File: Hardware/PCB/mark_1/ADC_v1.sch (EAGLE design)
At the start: 17 parts, among them IC1 MCP3424, IC2 MCP23017SO, Q1 IRLML6402, Q2 IRLML6402, Q3 IRLML6402, Q4 IRLML6402

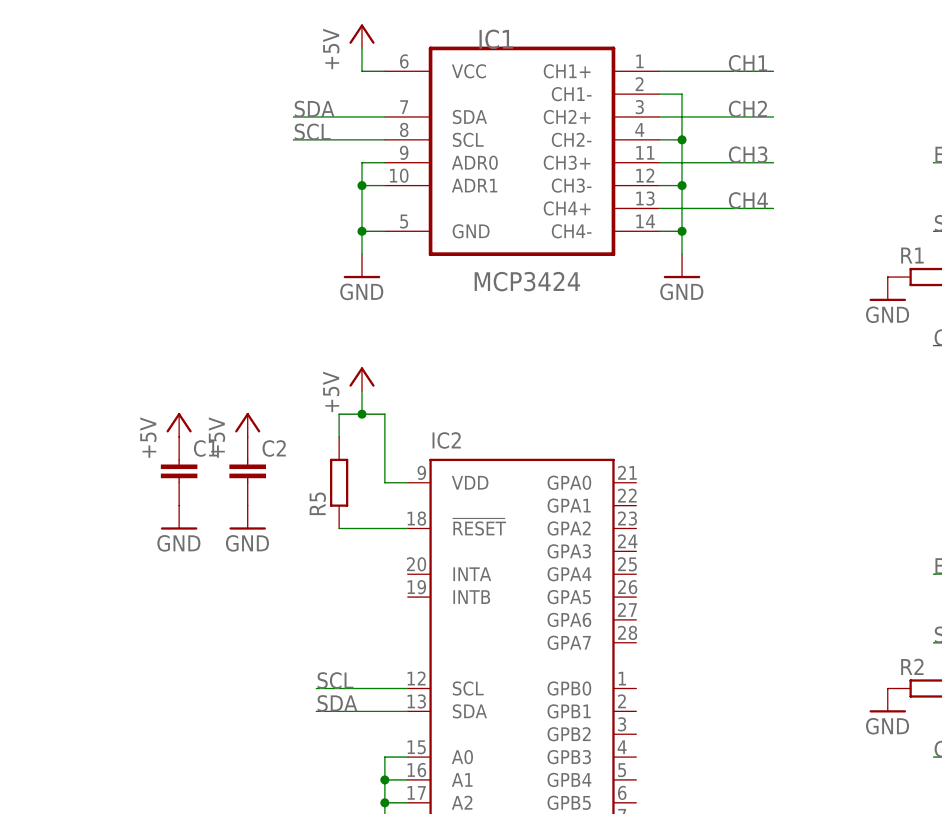
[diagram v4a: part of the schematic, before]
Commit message: 
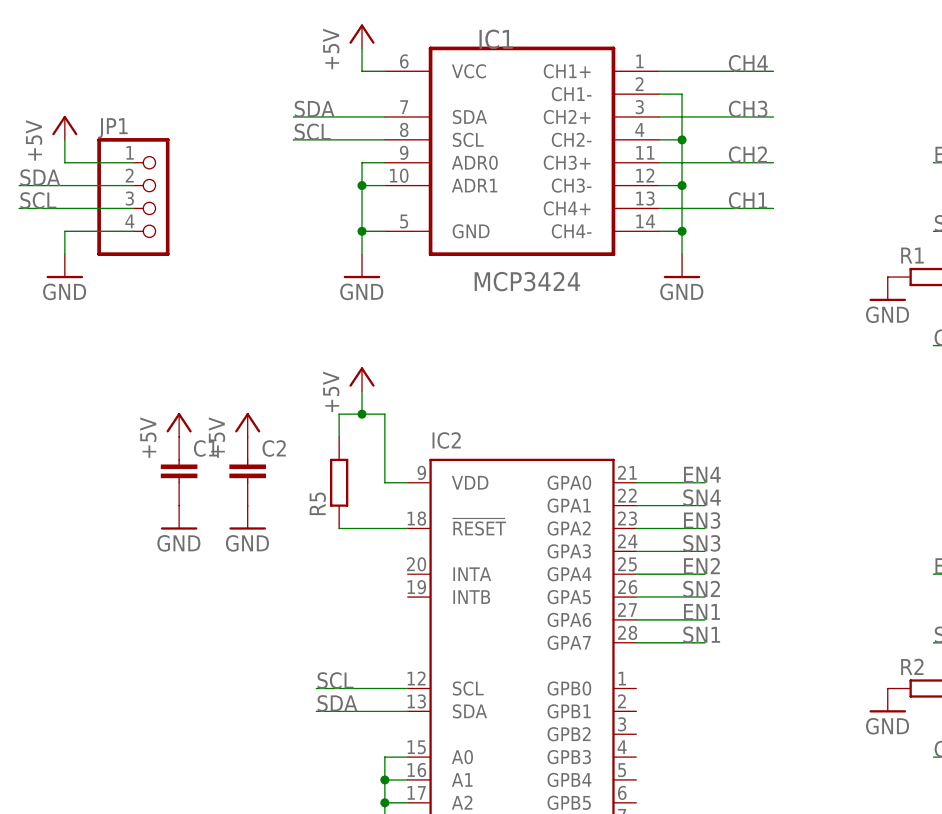
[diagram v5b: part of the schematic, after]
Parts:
- added JP1: (no value), mark_1:PINHD-1X4
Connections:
- net +5V: now also JP1.1
- net CH1: now also IC1.CH4+; no longer IC1.CH1+
- net CH2: now also IC1.CH3+; no longer IC1.CH2+
- net CH3: now also IC1.CH2+; no longer IC1.CH3+
- net CH4: now also IC1.CH1+; no longer IC1.CH4+
- net EN1: now also IC2.GPA6
- net EN2: now also IC2.GPA4
- net EN3: now also IC2.GPA2
- net EN4: now also IC2.GPA0
- net GND: now also JP1.4
- net SCL: now also JP1.3
- net SDA: now also JP1.2
- net SN1: now also IC2.GPA7
- net SN2: now also IC2.GPA5
- net SN3: now also IC2.GPA3
- net SN4: now also IC2.GPA1
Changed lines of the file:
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@@
 <part name="GND13" library="mark_1" deviceset="GND" device=""/>
 <part name="R5" library="mark_1" deviceset="R-EU_" device="R0805"/>
+<part name="JP1" library="mark_1" deviceset="PINHD-1X4" device=""/>
+<part name="P+9" library="mark_1" deviceset="+5V" device=""/>
+<part name="GND14" library="mark_1" deviceset="GND" device=""/>
 </parts>
 <sheets>
@@
 <instance part="GND13" gate="1" x="-15.24" y="17.78"/>
 <instance part="R5" gate="G$1" x="-127" y="43.18" rot="R90"/>
+<instance part="JP1" gate="A" x="-147.32" y="73.66"/>
+<instance part="P+9" gate="1" x="-157.48" y="83.82"/>
+<instance part="GND14" gate="1" x="-157.48" y="66.04"/>
 </instances>
 <busses>
@@
 <pinref part="Q4" gate="G$1" pin="S"/>
 <pinref part="P+8" gate="1" pin="+5V"/>
+</segment>
+<segment>
+<pinref part="JP1" gate="A" pin="1"/>
+<pinref part="P+9" gate="1" pin="+5V"/>
+<wire x1="-157.48" y1="81.28" x2="-157.48" y2="78.74" width="0.1524" layer="91"/>
+<wire x1="-157.48" y1="78.74" x2="-149.86" y2="78.74" width="0.1524" layer="91"/>
 </segment>
 </net>
@@
 <pinref part="GND13" gate="1" pin="GND"/>
 </segment>
+<segment>
+<pinref part="JP1" gate="A" pin="4"/>
+<pinref part="GND14" gate="1" pin="GND"/>
+<wire x1="-157.48" y1="68.58" x2="-157.48" y2="71.12" width="0.1524" layer="91"/>
+<wire x1="-157.48" y1="71.12" x2="-149.86" y2="71.12" width="0.1524" layer="91"/>
+</segment>
 </net>
 <net name="CH1" class="0">
-<segment>
-<pinref part="IC1" gate="A" pin="CH1+"/>
-<wire x1="-91.44" y1="88.9" x2="-78.74" y2="88.9" width="0.1524" layer="91"/>
-<label x="-83.82" y="88.9" size="1.778" layer="95"/>
-</segment>
 <segment>
 <pinref part="JK1" gate="G$1" pin="RING"/>
@@
 <label x="-60.96" y="58.42" size="1.778" layer="95"/>
 </segment>
+<segment>
+<pinref part="IC1" gate="A" pin="CH4+"/>
+<wire x1="-91.44" y1="73.66" x2="-78.74" y2="73.66" width="0.1524" layer="91"/>
+<label x="-83.82" y="73.66" size="1.778" layer="95"/>
+</segment>
 </net>
 <net name="CH2" class="0">
-<segment>
-<pinref part="IC1" gate="A" pin="CH2+"/>
-<wire x1="-91.44" y1="83.82" x2="-78.74" y2="83.82" width="0.1524" layer="91"/>
-<label x="-83.82" y="83.82" size="1.778" layer="95"/>
-</segment>
 <segment>
 <pinref part="JK2" gate="G$1" pin="RING"/>
@@
 <label x="-60.96" y="12.7" size="1.778" layer="95"/>
 </segment>
-</net>
-<net name="CH3" class="0">
 <segment>
 <pinref part="IC1" gate="A" pin="CH3+"/>
@@
 <label x="-83.82" y="78.74" size="1.778" layer="95"/>
 </segment>
+</net>
+<net name="CH3" class="0">
 <segment>
 <pinref part="JK3" gate="G$1" pin="RING"/>
@@
 <label x="-10.16" y="58.42" size="1.778" layer="95"/>
 </segment>
+<segment>
+<pinref part="IC1" gate="A" pin="CH2+"/>
+<wire x1="-91.44" y1="83.82" x2="-78.74" y2="83.82" width="0.1524" layer="91"/>
+<label x="-83.82" y="83.82" size="1.778" layer="95"/>
+</segment>
 </net>
 <net name="CH4" class="0">
-<segment>
-<pinref part="IC1" gate="A" pin="CH4+"/>
-<wire x1="-91.44" y1="73.66" x2="-78.74" y2="73.66" width="0.1524" layer="91"/>
-<label x="-83.82" y="73.66" size="1.778" layer="95"/>
-</segment>
 <segment>
 <pinref part="JK4" gate="G$1" pin="RING"/>
@@
 <label x="-10.16" y="12.7" size="1.778" layer="95"/>
 </segment>
+<segment>
+<pinref part="IC1" gate="A" pin="CH1+"/>
+<wire x1="-91.44" y1="88.9" x2="-78.74" y2="88.9" width="0.1524" layer="91"/>
+<label x="-83.82" y="88.9" size="1.778" layer="95"/>
+</segment>
 </net>
 <net name="SDA" class="0">
@@
 <label x="-129.54" y="17.78" size="1.778" layer="95"/>
 </segment>
+<segment>
+<pinref part="JP1" gate="A" pin="2"/>
+<wire x1="-149.86" y1="76.2" x2="-162.56" y2="76.2" width="0.1524" layer="91"/>
+<label x="-162.56" y="76.2" size="1.778" layer="95"/>
+</segment>
 </net>
 <net name="SCL" class="0">
@@
 <wire x1="-119.38" y1="20.32" x2="-129.54" y2="20.32" width="0.1524" layer="91"/>
 <label x="-129.54" y="20.32" size="1.778" layer="95"/>
+</segment>
+<segment>
+<pinref part="JP1" gate="A" pin="3"/>
+<wire x1="-149.86" y1="73.66" x2="-162.56" y2="73.66" width="0.1524" layer="91"/>
+<label x="-162.56" y="73.66" size="1.778" layer="95"/>
 </segment>
 </net>
@@
 <label x="-60.96" y="78.74" size="1.778" layer="95"/>
 </segment>
+<segment>
+<pinref part="IC2" gate="G$1" pin="GPA6"/>
+<wire x1="-93.98" y1="27.94" x2="-86.36" y2="27.94" width="0.1524" layer="91"/>
+<label x="-88.9" y="27.94" size="1.778" layer="95"/>
+</segment>
 </net>
 <net name="EN3" class="0">
@@
 <label x="-10.16" y="78.74" size="1.778" layer="95"/>
 </segment>
+<segment>
+<pinref part="IC2" gate="G$1" pin="GPA2"/>
+<wire x1="-93.98" y1="38.1" x2="-86.36" y2="38.1" width="0.1524" layer="91"/>
+<label x="-88.9" y="38.1" size="1.778" layer="95"/>
+</segment>
 </net>
 <net name="EN2" class="0">
@@
 <label x="-60.96" y="33.02" size="1.778" layer="95"/>
 </segment>
+<segment>
+<pinref part="IC2" gate="G$1" pin="GPA4"/>
+<wire x1="-93.98" y1="33.02" x2="-86.36" y2="33.02" width="0.1524" layer="91"/>
+<label x="-88.9" y="33.02" size="1.778" layer="95"/>
+</segment>
 </net>
 <net name="EN4" class="0">
@@
 <wire x1="-2.54" y1="33.02" x2="-10.16" y2="33.02" width="0.1524" layer="91"/>
 <label x="-10.16" y="33.02" size="1.778" layer="95"/>
+</segment>
+<segment>
+<pinref part="IC2" gate="G$1" pin="GPA0"/>
+<wire x1="-93.98" y1="43.18" x2="-86.36" y2="43.18" width="0.1524" layer="91"/>
+<label x="-88.9" y="43.18" size="1.778" layer="95"/>
 </segment>
 </net>
@@
 <label x="-60.96" y="71.12" size="1.778" layer="95"/>
 </segment>
+<segment>
+<pinref part="IC2" gate="G$1" pin="GPA7"/>
+<wire x1="-93.98" y1="25.4" x2="-86.36" y2="25.4" width="0.1524" layer="91"/>
+<label x="-88.9" y="25.4" size="1.778" layer="95"/>
+</segment>
 </net>
 <net name="SN2" class="0">
@@
 <label x="-60.96" y="25.4" size="1.778" layer="95"/>
 </segment>
+<segment>
+<pinref part="IC2" gate="G$1" pin="GPA5"/>
+<wire x1="-93.98" y1="30.48" x2="-86.36" y2="30.48" width="0.1524" layer="91"/>
+<label x="-88.9" y="30.48" size="1.778" layer="95"/>
+</segment>
 </net>
 <net name="SN3" class="0">
@@
 <label x="-10.16" y="71.12" size="1.778" layer="95"/>
 </segment>
+<segment>
+<pinref part="IC2" gate="G$1" pin="GPA3"/>
+<wire x1="-93.98" y1="35.56" x2="-86.36" y2="35.56" width="0.1524" layer="91"/>
+<label x="-88.9" y="35.56" size="1.778" layer="95"/>
+</segment>
 </net>
 <net name="SN4" class="0">
@@
 <label x="-10.16" y="25.4" size="1.778" layer="95"/>
 </segment>
-</net>
+<segment>
+<pinref part="IC2" gate="G$1" pin="GPA1"/>
+<wire x1="-93.98" y1="40.64" x2="-86.36" y2="40.64" width="0.1524" layer="91"/>
+<label x="-88.9" y="40.64" size="1.778" layer="95"/>
+</segment>
+</net>

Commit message: 
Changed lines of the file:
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@@
 <instance part="GND1" gate="1" x="-88.9" y="66.04"/>
 <instance part="IC1" gate="A" x="-106.68" y="81.28"/>
-<instance part="P+2" gate="1" x="-124.46" y="93.98"/>
+<instance part="P+2" gate="1" x="-124.46" y="93.98" smashed="yes">
+<attribute name="VALUE" x="-121.92" y="96.52" size="1.778" layer="96" rot="R180"/>
+</instance>
 <instance part="GND2" gate="1" x="-124.46" y="66.04"/>
 <instance part="C1" gate="G$1" x="-144.78" y="45.72"/>
-<instance part="P+3" gate="1" x="-144.78" y="50.8"/>
+<instance part="P+3" gate="1" x="-144.78" y="50.8" smashed="yes">
+<attribute name="VALUE" x="-142.24" y="53.34" size="1.778" layer="96" rot="R180"/>
+</instance>
 <instance part="GND3" gate="1" x="-144.78" y="38.1"/>
 <instance part="IC2" gate="G$1" x="-106.68" y="22.86"/>
 <instance part="GND5" gate="1" x="-121.92" y="-2.54"/>
-<instance part="P+4" gate="1" x="-124.46" y="55.88"/>
+<instance part="P+4" gate="1" x="-124.46" y="55.88" smashed="yes">
+<attribute name="VALUE" x="-121.92" y="58.42" size="1.778" layer="96" rot="R180"/>
+</instance>
 <instance part="C2" gate="G$1" x="-137.16" y="45.72"/>
-<instance part="P+5" gate="1" x="-137.16" y="50.8"/>
+<instance part="P+5" gate="1" x="-137.16" y="50.8" smashed="yes">
+<attribute name="VALUE" x="-134.62" y="53.34" size="1.778" layer="96" rot="R180"/>
+</instance>
 <instance part="GND6" gate="1" x="-137.16" y="38.1"/>
 <instance part="JK1" gate="G$1" x="-40.64" y="63.5" rot="R180"/>
@@
 <instance part="R5" gate="G$1" x="-127" y="43.18" rot="R90"/>
 <instance part="JP1" gate="A" x="-147.32" y="73.66"/>
-<instance part="P+9" gate="1" x="-157.48" y="83.82"/>
+<instance part="P+9" gate="1" x="-157.48" y="83.82" smashed="yes">
+<attribute name="VALUE" x="-154.94" y="86.36" size="1.778" layer="96" rot="R180"/>
+</instance>
 <instance part="GND14" gate="1" x="-157.48" y="66.04"/>
 </instances>

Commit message: 
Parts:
- IC2: value MCP23017SO -> MCP23017
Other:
- moved on the sheet: C1, C2
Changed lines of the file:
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@@
 <part name="P+3" library="mark_1" deviceset="+5V" device=""/>
 <part name="GND3" library="mark_1" deviceset="GND" device=""/>
-<part name="IC2" library="mark_1" deviceset="MCP23017" device="SO"/>
+<part name="IC2" library="mark_1" deviceset="MCP23017" device="SO" value="MCP23017"/>
 <part name="GND5" library="mark_1" deviceset="GND" device=""/>
 <part name="P+4" library="mark_1" deviceset="+5V" device=""/>
@@
 </instance>
 <instance part="GND2" gate="1" x="-124.46" y="66.04"/>
-<instance part="C1" gate="G$1" x="-144.78" y="45.72"/>
-<instance part="P+3" gate="1" x="-144.78" y="50.8" smashed="yes">
-<attribute name="VALUE" x="-142.24" y="53.34" size="1.778" layer="96" rot="R180"/>
+<instance part="C1" gate="G$1" x="-157.48" y="43.18"/>
+<instance part="P+3" gate="1" x="-157.48" y="48.26" smashed="yes">
+<attribute name="VALUE" x="-154.94" y="50.8" size="1.778" layer="96" rot="R180"/>
 </instance>
-<instance part="GND3" gate="1" x="-144.78" y="38.1"/>
+<instance part="GND3" gate="1" x="-157.48" y="35.56"/>
 <instance part="IC2" gate="G$1" x="-106.68" y="22.86"/>
 <instance part="GND5" gate="1" x="-121.92" y="-2.54"/>
@@
 <attribute name="VALUE" x="-121.92" y="58.42" size="1.778" layer="96" rot="R180"/>
 </instance>
-<instance part="C2" gate="G$1" x="-137.16" y="45.72"/>
-<instance part="P+5" gate="1" x="-137.16" y="50.8" smashed="yes">
-<attribute name="VALUE" x="-134.62" y="53.34" size="1.778" layer="96" rot="R180"/>
+<instance part="C2" gate="G$1" x="-149.86" y="43.18"/>
+<instance part="P+5" gate="1" x="-149.86" y="48.26" smashed="yes">
+<attribute name="VALUE" x="-147.32" y="50.8" size="1.778" layer="96" rot="R180"/>
 </instance>
-<instance part="GND6" gate="1" x="-137.16" y="38.1"/>
+<instance part="GND6" gate="1" x="-149.86" y="35.56"/>
 <instance part="JK1" gate="G$1" x="-40.64" y="63.5" rot="R180"/>
 <instance part="GND7" gate="1" x="-48.26" y="53.34"/>
